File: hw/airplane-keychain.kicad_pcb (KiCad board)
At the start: 2 copper layers, 103.1 x 141.7 mm, 21 parts, among them IC1 ATTINY85-P, SW1 SW_PUSH, SW2 SPST

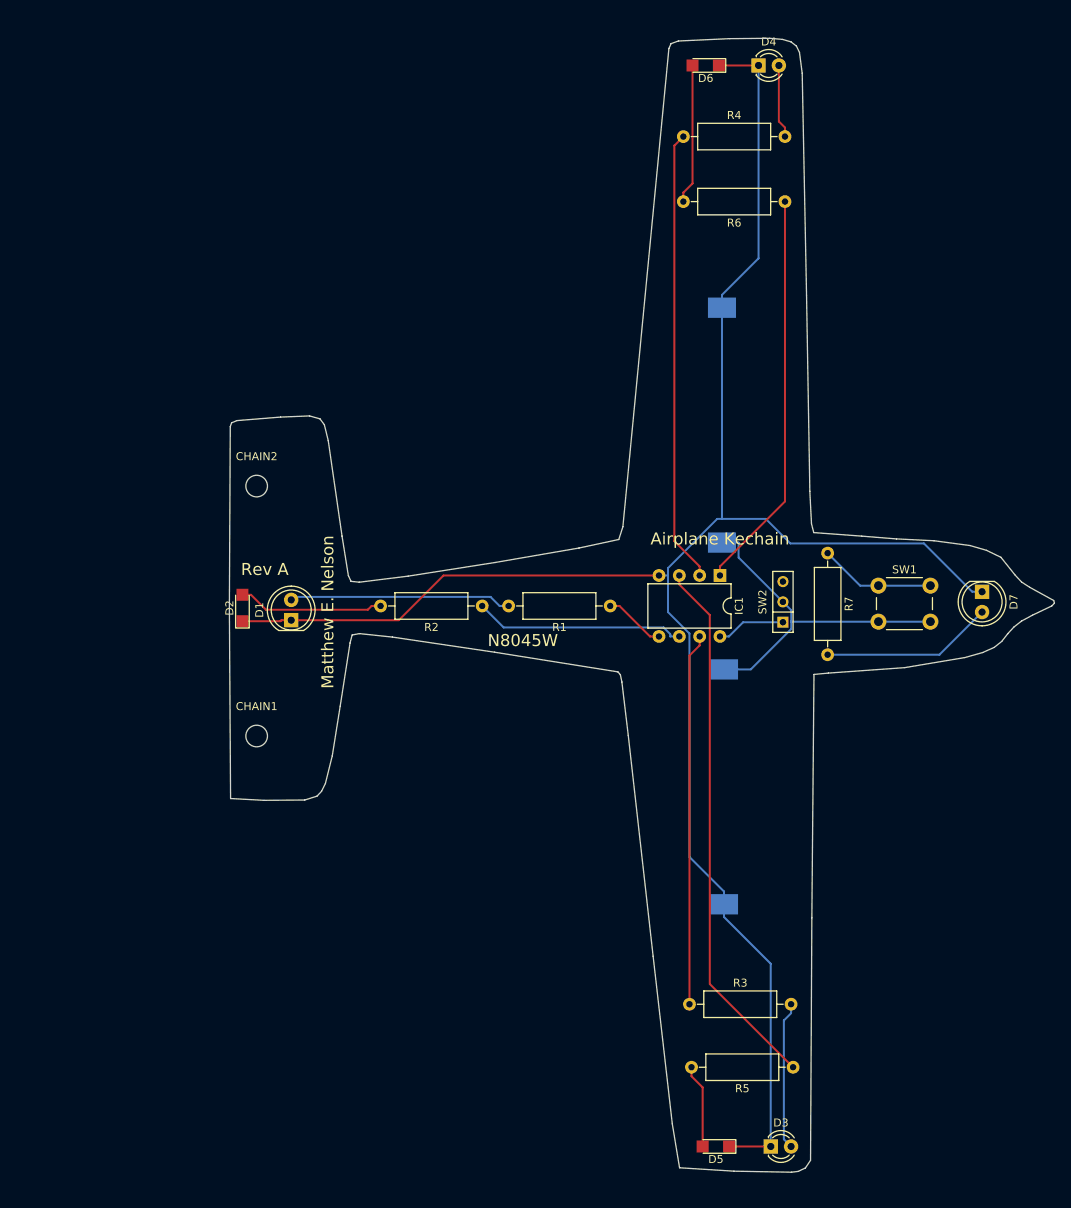
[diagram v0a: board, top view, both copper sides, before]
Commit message: Final for RevA
Final changes based on prototype testing for Rev A.
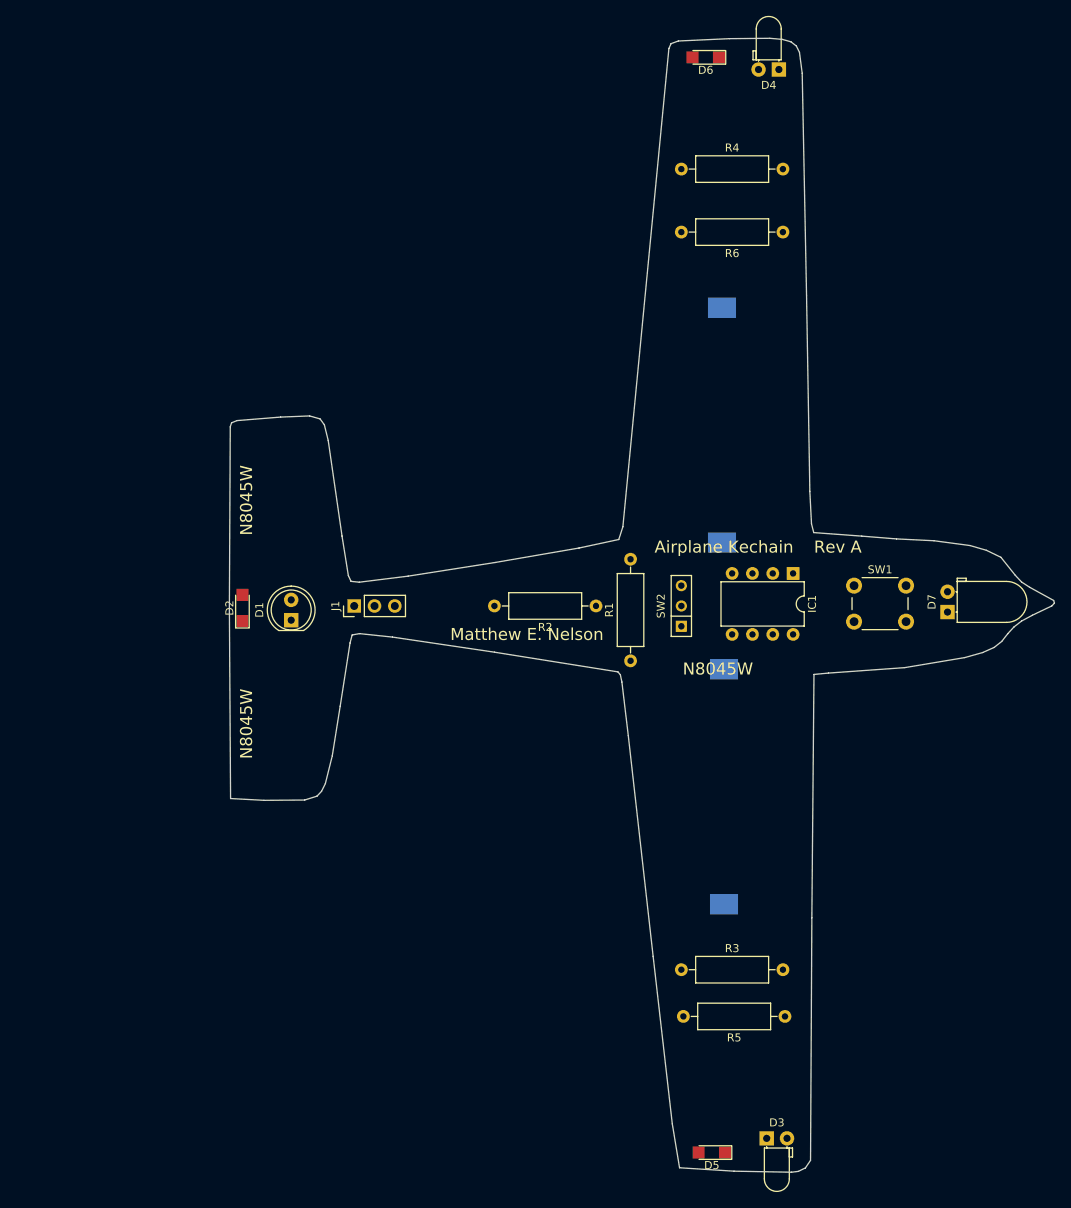
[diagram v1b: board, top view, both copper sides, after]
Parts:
- removed CHAIN1, CHAIN2: MountingHole_2.7mm, Mounting_Holes:MountingHole_2.7mm
- removed R7: 50, Resistors_THT:R_Axial_DIN0309_L9.0mm_D3.2mm_P12.70mm_Horizontal
- added J1: CONN_01X03_MALE, Pin_Headers:Pin_Header_Straight_1x03_Pitch2.54mm, F.Cu at (96.8, 95.8)
- D3, D4: footprint LEDs:LED_D3.0mm -> LEDs:LED_D3.0mm_Horizontal_O1.27mm_Z2.0mm
- D7: footprint LEDs:LED_D5.0mm -> LEDs:LED_D5.0mm_Horizontal_O1.27mm_Z3.0mm
- R5: value 100 -> 50
- R6: value 100 -> 10k
- moved R2 14.2 mm to (127.0, 95.8)
- moved SW2 12.7 mm to (137.7, 95.8)
- moved IC1 9.15 mm to (151.6, 91.7)
- moved R1 7.31 mm to (131.3, 102.6), turned to 90 degrees
- moved R5 6.43 mm to (150.6, 147.1)
- moved D7 5.01 mm to (170.9, 96.5), turned to 90 degrees
- moved R3 4.44 mm to (137.7, 141.2)
- moved R4 4.07 mm to (137.7, 41.1)
- moved R6 3.82 mm to (150.4, 49.0)
- moved SW1 3.05 mm to (159.3, 93.2)
- moved D4 2.59 mm to (149.9, 28.7), turned to 180 degrees
- moved D3 1.14 mm to (148.3, 162.3)
- moved D6 1.02 mm to (140.7, 27.2)
- moved D5 0.92 mm to (141.5, 164.1)
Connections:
- D6 pad 2: Net-(D6-Pad2) -> Net-(D5-Pad2)
- IC1 pad 3: Net-(IC1-Pad3) -> Net-(D5-Pad2)
- R5 pad 1: Net-(IC1-Pad3) -> Net-(R5-Pad1)
- R5 pad 2: Net-(D5-Pad2) -> Net-(D7-Pad2)
- R6 pad 1: Net-(IC1-Pad1) -> Net-(IC1-Pad8)
- R6 pad 2: Net-(D6-Pad2) -> Net-(IC1-Pad1)
- SW1 pad 1: Net-(R7-Pad1) -> Net-(R5-Pad1)
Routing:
- net GND: track 247.5 -> 0.00 mm
- net Net-(IC1-Pad3): track 67.4 -> 0.00 mm
- net Net-(IC1-Pad2): track 56.6 -> 0.00 mm
- net Net-(IC1-Pad1): track 50.1 -> 0.00 mm
- net Net-(IC1-Pad7): track 46.5 -> 0.00 mm
- net Net-(BT1-Pad1): track 43.5 -> 0.00 mm
- net Net-(D1-Pad2): track 27.8 -> 0.00 mm
- net Net-(IC1-Pad6): track 26.4 -> 0.00 mm
- net Net-(D7-Pad2): track 21.5 -> 0.00 mm
- net Net-(D3-Pad2): track 18.5 -> 0.00 mm
- net Net-(D2-Pad2): track 18.2 -> 0.00 mm
- net Net-(D6-Pad2): track 17.5 -> 0.00 mm
- net Net-(R7-Pad1): track 14.5 -> 0.00 mm
- net Net-(D5-Pad2): track 10.5 -> 0.00 mm
- net Net-(D4-Pad2): track 9.21 -> 0.00 mm
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
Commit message: Update to newer KiCad
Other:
- net class Default removed

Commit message: Initial update for ISGC model
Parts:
- removed IC1: ATTINY85-P, Housings_DIP:DIP-8_W7.62mm
- added G***: LOGO, LOGO, F.Cu at (130.5, 95.6)
- added R7: 100, Resistor_THT:R_Axial_DIN0309_L9.0mm_D3.2mm_P12.70mm_Horizontal, F.Cu at (140.9, 76.7)
- added R8: 100, Resistor_THT:R_Axial_DIN0309_L9.0mm_D3.2mm_P12.70mm_Horizontal, F.Cu at (144.2, 69.0)
- added R9: 100, Resistor_THT:R_Axial_DIN0309_L9.0mm_D3.2mm_P12.70mm_Horizontal, F.Cu at (158.2, 73.7)
- added U1: ATtiny85-20P, Package_DIP:DIP-8_W7.62mm, F.Cu at (111.8, 85.6)
- BT1, BT2: footprint Battery_Holders:Keystone_1058_1x2032-CoinCell -> Battery:BatteryHolder_Keystone_1058_1x2032
- D1: footprint LEDs:LED_D5.0mm -> LED_THT:LED_D3.0mm
- D2, D5, D6: footprint LEDs:LED_1206 -> LED_THT:LED_D3.0mm
- D3, D4: footprint LEDs:LED_D3.0mm_Horizontal_O1.27mm_Z2.0mm -> LED_THT:LED_D3.0mm
- D7: footprint LEDs:LED_D5.0mm_Horizontal_O1.27mm_Z3.0mm -> LED_THT:LED_D3.0mm
- J1: footprint Pin_Headers:Pin_Header_Straight_1x03_Pitch2.54mm -> Connector_PinHeader_2.54mm:PinHeader_1x03_P2.54mm_Horizontal
- R1, R2, R3, R4, R5, R6: footprint Resistors_THT:R_Axial_DIN0309_L9.0mm_D3.2mm_P12.70mm_Horizontal -> Resistor_THT:R_Axial_DIN0309_L9.0mm_D3.2mm_P12.70mm_Horizontal
- SW1: footprint Buttons_Switches_THT:SW_PUSH_6mm -> Button_Switch_THT:SW_PUSH_6mm
- SW2: footprint Buttons_Switches_THT:SW_Micro_SPST -> Button_Switch_THT:SW_DIP_SPSTx01_Slide_9.78x4.72mm_W7.62mm_P2.54mm
- moved D3 97.3 mm to (116.8, 70.3)
- moved D5 89.8 mm to (115.2, 78.2)
- moved R5 86.9 mm to (95.7, 79.8), turned to -90 degrees
- moved D4 79.9 mm to (162.5, 107.6)
- moved D1 79.2 mm to (165.6, 117.1)
- moved R4 72.2 mm to (94.2, 98.8)
- moved R6 70.6 mm to (107.2, 104.8)
- moved D6 60.1 mm to (105.8, 76.1)
- moved R3 57.3 mm to (156.7, 87.2)
- moved SW2 39.9 mm to (173.6, 113.0), turned to -90 degrees
- moved D2 38.1 mm to (112.5, 72.2), turned to 180 degrees
- moved R1 38.0 mm to (167.9, 92.5), turned to -90 degrees
- moved SW1 28.3 mm to (149.1, 119.6)
- moved R2 25.3 mm to (107.2, 111.5)
- moved D7 23.8 mm to (157.0, 115.8)
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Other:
- board size 103.1 x 141.7 mm -> 93.7 x 109.7 mm
- board text removed: "Airplane Kechain"
- board text removed: "N8045W"
- board text removed: "Rev A"

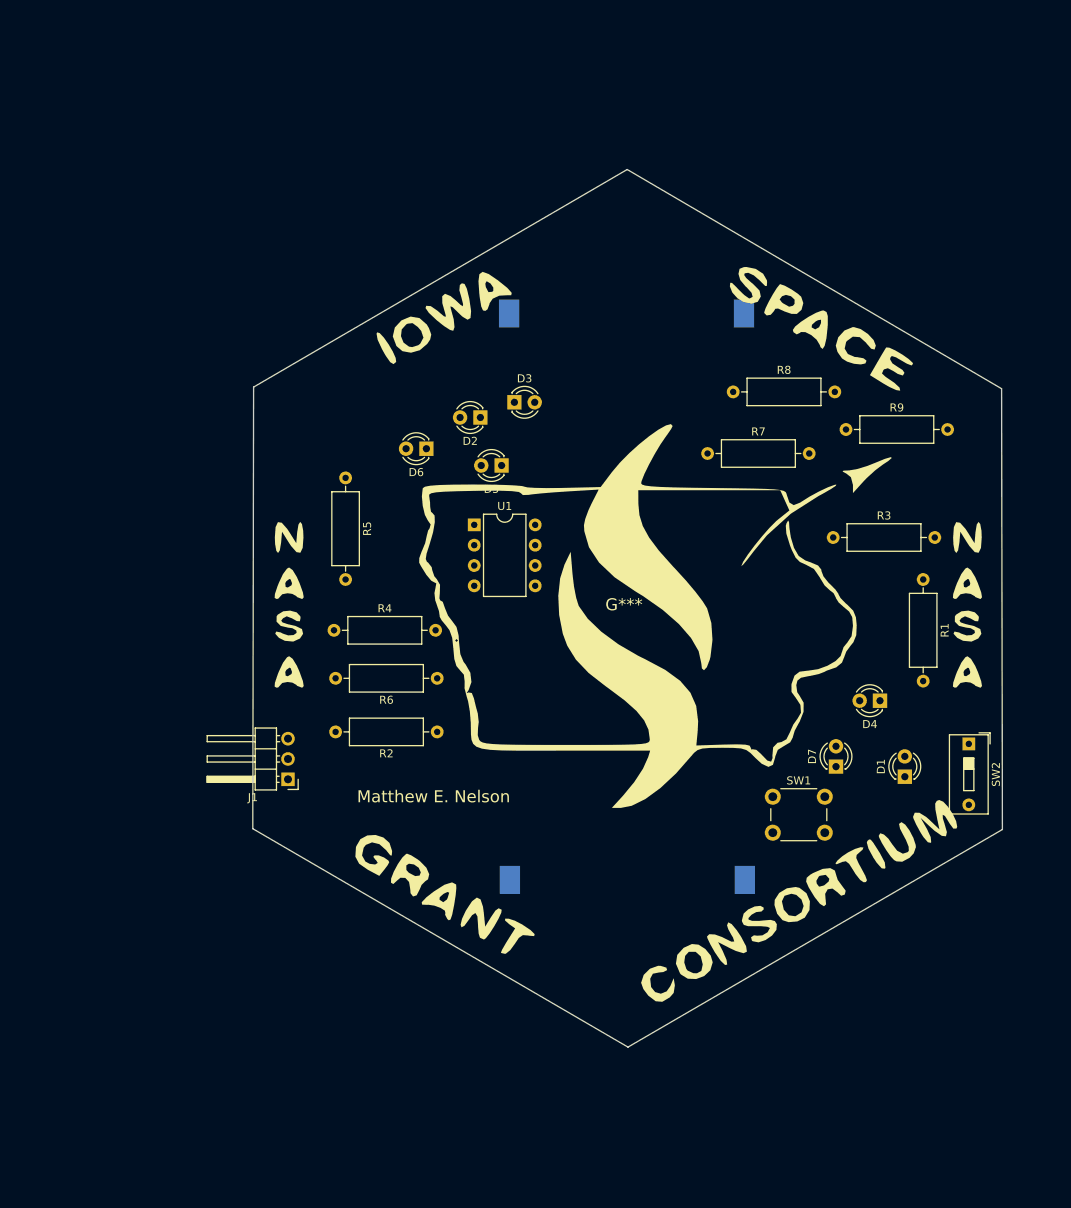
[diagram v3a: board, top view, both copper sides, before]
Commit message: Updates to logo
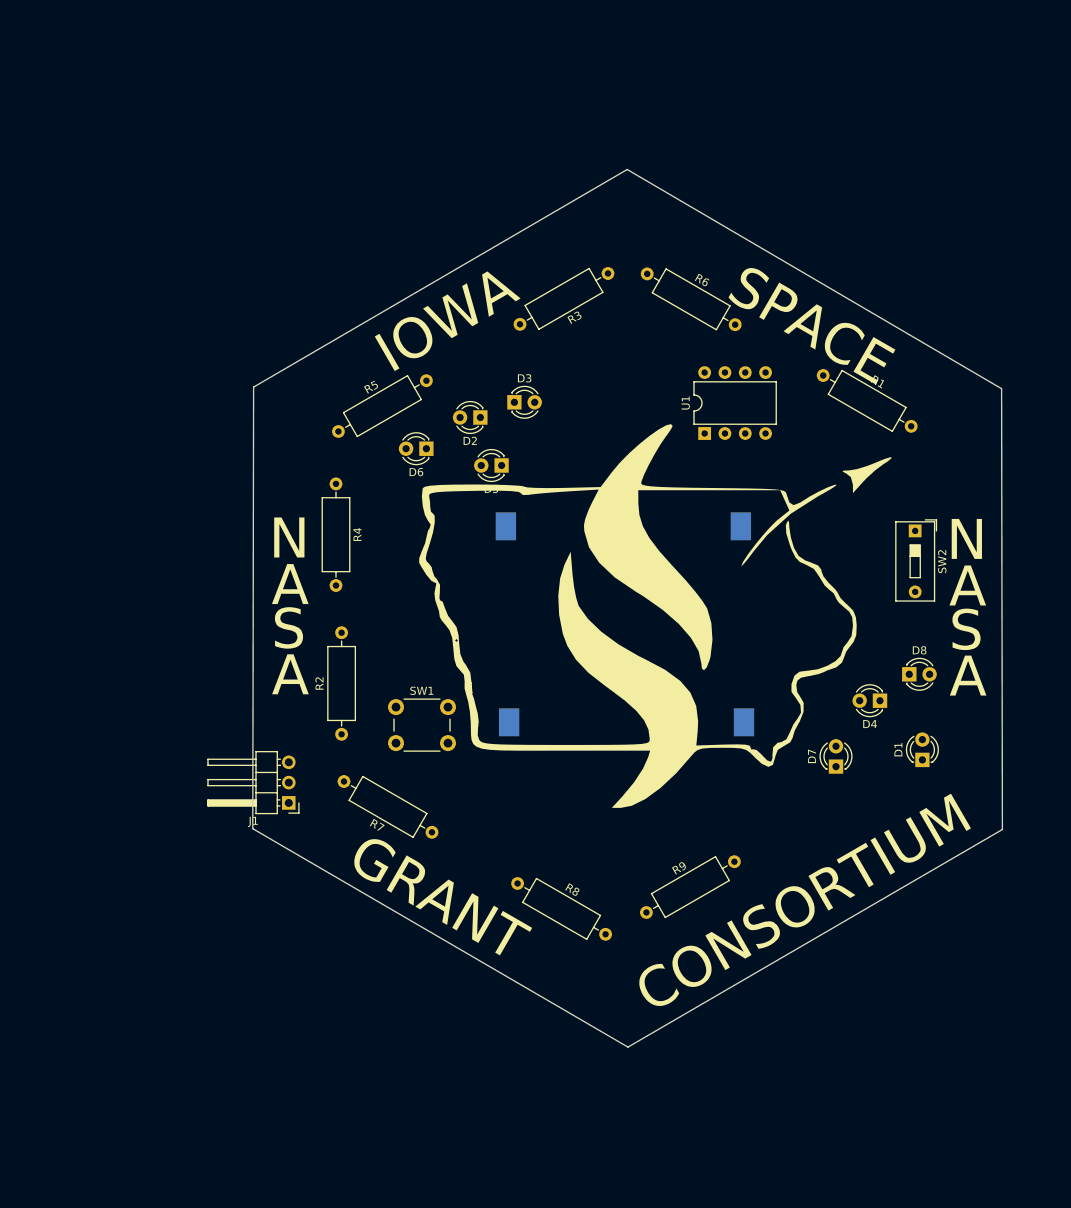
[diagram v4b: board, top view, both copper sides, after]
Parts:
- added D8: LED, LED_THT:LED_D3.0mm, F.Cu at (166.2, 104.3)
- R5: value 50 -> 100
- moved R8 67.1 mm to (117.2, 130.4), turned to -30 degrees
- moved R9 65.3 mm to (133.3, 134.1), turned to 30 degrees
- moved R7 58.6 mm to (106.5, 124.0), turned to 150 degrees
- moved R6 57.0 mm to (133.4, 54.2), turned to -30 degrees
- moved SW1 48.4 mm to (102.0, 108.4)
- moved R3 43.4 mm to (128.5, 54.2), turned to -150 degrees
- moved U1 31.0 mm to (140.6, 74.2), turned to 90 degrees
- moved R1 28.4 mm to (155.4, 67.0), turned to -30 degrees
- moved SW2 27.5 mm to (166.9, 86.4)
- moved BT1 26.6 mm to (130.4, 85.8)
- moved BT2 19.7 mm to (130.8, 110.3)
- moved R4 18.3 mm to (94.5, 80.5), turned to -90 degrees
- moved R2 12.0 mm to (95.2, 111.8), turned to 90 degrees
- moved R5 5.87 mm to (94.8, 74.0), turned to 30 degrees
- moved D1 3.04 mm to (167.8, 115.0)
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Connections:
- D6 pad 2: Net-(D5-A) -> Net-(D6-A)
- R7 pad 1: unconnected-(R7-Pad1) -> Net-(U1-XTAL2/PB4)
- R7 pad 2: unconnected-(R7-Pad2) -> Net-(D5-A)
- R8 pad 1: unconnected-(R8-Pad1) -> Net-(U1-XTAL2/PB4)
- R8 pad 2: unconnected-(R8-Pad2) -> Net-(D6-A)
- R9 pad 1: unconnected-(R9-Pad1) -> Net-(R5-Pad1)
- R9 pad 2: unconnected-(R9-Pad2) -> Net-(D8-A)
- U1 pad 3: Net-(D5-A) -> Net-(U1-XTAL2/PB4)
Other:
- board text added: "ISGC Badge Rev A Matthew E. Nelson"
- board text removed: "Matthew E. Nelson"

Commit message: Update for ISGC
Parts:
- removed J1: CONN_01X03_MALE, Connector_PinHeader_2.54mm:PinHeader_1x03_P2.54mm_Horizontal
- added H1: MountingHole, MountingHole:MountingHole_4.3mm_M4, F.Cu at (130.8, 46.6)
- moved R5 77.8 mm to (153.1, 125.5)
- moved R4 72.5 mm to (167.0, 82.3)
- moved SW2 71.4 mm to (95.6, 82.2)
- moved R2 47.4 mm to (108.3, 66.2), turned to -150 degrees
- moved SW1 4.90 mm to (100.3, 103.8), turned to 180 degrees
- moved R9 2.65 mm to (133.8, 136.7)
- turned BT2 to 180 degrees
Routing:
- net Net-(BT1-+): track 0.00 -> 92.2 mm
- net Net-(D6-A): track 0.00 -> 91.9 mm
- net Net-(R5-Pad1): track 0.00 -> 86.7 mm
- net Net-(U1-XTAL2/PB4): track 0.00 -> 77.6 mm
- net Net-(U1-VCC): track 0.00 -> 66.7 mm
- net Net-(D5-A): track 0.00 -> 58.1 mm
- net Net-(U1-PB1): track 0.00 -> 52.4 mm
- net Net-(D1-A): track 0.00 -> 41.5 mm
- net Net-(D8-A): track 0.00 -> 38.5 mm
- net Net-(U1-XTAL1/PB3): track 0.00 -> 28.2 mm
- net Net-(U1-PB2): track 0.00 -> 23.1 mm
- net Net-(D4-A): track 0.00 -> 15.5 mm
- net Net-(U1-~{RESET}/PB5): track 0.00 -> 15.2 mm
- net Net-(D2-A): track 0.00 -> 12.9 mm
- net Net-(D3-A): track 0.00 -> 10.5 mm
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- added copper zone on B.Cu, net GND
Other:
- rule pad_to_mask_clearance: 0.2 -> 0

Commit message: Updates
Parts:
- added D9: LED, LED_THT:LED_D3.0mm, F.Cu at (162.6, 99.1)
- added R10: 100, Resistor_THT:R_Axial_DIN0309_L9.0mm_D3.2mm_P12.70mm_Horizontal, F.Cu at (129.5, 124.5)
- moved R5 4.24 mm to (149.4, 127.6)
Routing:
- net Net-(D8-A): track 38.5 -> 0.00 mm
- net Net-(R10-Pad1): track 86.7 -> 62.8 mm
- net Net-(D7-A): track 9.52 -> 0.00 mm
